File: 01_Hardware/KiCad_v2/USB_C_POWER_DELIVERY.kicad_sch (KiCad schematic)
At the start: 29 parts, among them Q200 SI7615DN-T1-GE3, Q201 SI7615DN-T1-GE3, Q202 DMP6050SSD, Q203 NVTA7002NT1G, U200 CYPD3177-24LQ

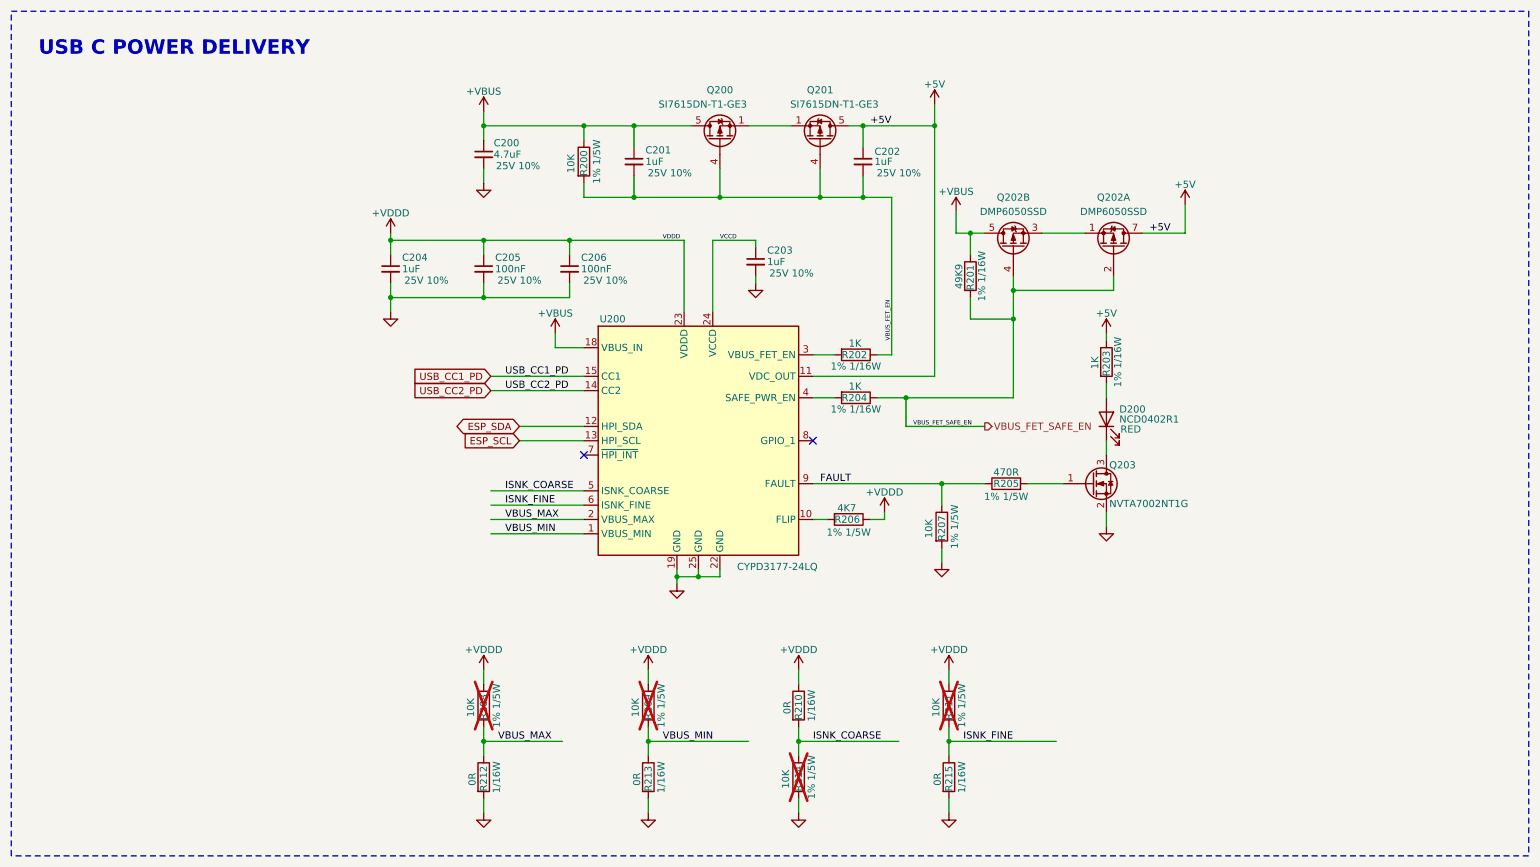
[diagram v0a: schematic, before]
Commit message: BOM done, except connectors/thermistor/button -> Will re-check BOM before sending to manufacturing
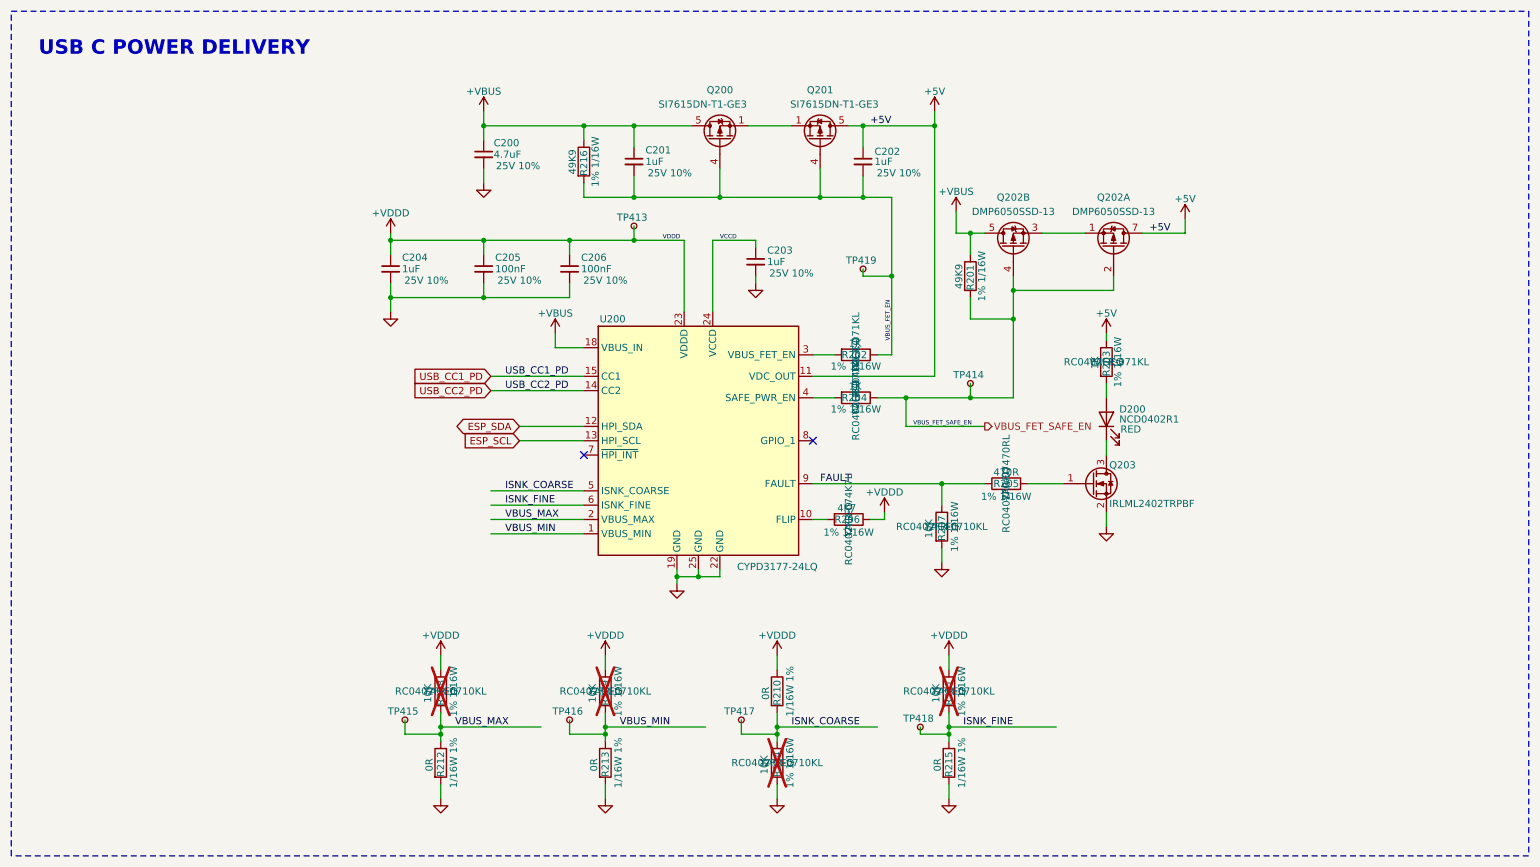
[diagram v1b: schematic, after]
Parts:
- removed R200: 10K, Resistor_SMD:R_0402_1005Metric, symbol Device:R
- added R216: 49K9, Resistor_SMD:R_0402_1005Metric, symbol Device:R
- added TP413, TP414, TP415, TP416, TP417, TP418, TP419: TestPoint_Small, TestPoint:TestPoint_Pad_D1.5mm, symbol Connector:TestPoint_Small
- C205, C206: Manufacturer Samsung Electro-Mechanics -> Samsung Electro-Mechanics
- D200: footprint Custom_Global_Footprints:SML-P13PTT_LED_0402_1005Metric -> LED_SMD:LED_0402_1005Metric
- Q202: value DMP6050SSD -> DMP6050SSD-13; Manufacturer Diodes Incorporated -> Diodes Incorporated
- Q203: value NVTA7002NT1G -> IRLML2402TRPBF; footprint Custom_Global_Footprints:NVTA7002N -> Package_TO_SOT_SMD:SOT-23; Link (none) -> https://jlcpcb.com/partdetail/InfineonTechnologies-IRLML240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; Manufacturer (none) -> Infineon Technologies; Manufacturer Part Number (none) -> IRLML2402TRPBF
- R201: Manufacturer (none) -> YAGEO; Manufacturer Part Number (none) -> RC0402FR-0749K9L
- R202, R203, R204: Manufacturer (none) -> YAGEO; Manufacturer Part Number (none) -> RC0402FR-071KL
- R205: Manufacturer (none) -> YAGEO; Manufacturer Part Number (none) -> RC0402FR-07470RL
- R206: Manufacturer (none) -> YAGEO; Manufacturer Part Number (none) -> RC0402FR-074K7L
- R207, R208, R209, R211, R214: Manufacturer (none) -> YAGEO; Manufacturer Part Number (none) -> RC0402FR-0710KL
- R210, R212, R213, R215: Manufacturer (none) -> YAGEO; Manufacturer Part Number (none) -> AC0402FR-070RL
- U200: Link (none) -> https://jlcpcb.com/partdetail/3345638-CYPD317724LQXQ/C29593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; Manufacturer (none) -> Infineon/Cypress Semicon; Manufacturer Part Number (none) -> CYPD3177-24LQXQ
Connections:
- net +VBUS: now also R216.1
- net +VDDD: now also TP413.1
- net ISNK_COARSE: now also TP417.1
- net ISNK_FINE: now also TP418.1
- net VBUS_FET_EN: now also R216.2, TP419.1
- net VBUS_FET_SAFE_EN: now also TP414.1
- net VBUS_MAX: now also TP415.1
- net VBUS_MIN: now also TP416.1
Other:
- moved on the sheet: R208, R209, R210, R211, R212, R213, R214, R215

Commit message: USB-C and Serial PCB routing done
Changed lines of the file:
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@@
 					(size 1.27 1.27)
 				)
+				(hide yes)
 			)
 		)
@@
 					(size 1.27 1.27)
 				)
+				(hide yes)
 			)
 		)
@@
 					(size 1.27 1.27)
 				)
+				(hide yes)
 			)
 		)
@@
 					(size 1.27 1.27)
 				)
+				(hide yes)
 			)
 		)
@@
 					(size 1.27 1.27)
 				)
+				(hide yes)
 			)
 		)
@@
 					(size 1.27 1.27)
 				)
+				(hide yes)
 			)
 		)
@@
 					(size 1.27 1.27)
 				)
+				(hide yes)
 			)
 		)
@@
 					(size 1.27 1.27)
 				)
+				(hide yes)
 			)
 		)
@@
 					(size 1.27 1.27)
 				)
+				(hide yes)
 			)
 		)
@@
 					(size 1.27 1.27)
 				)
+				(hide yes)
 			)
 		)
@@
 					(size 1.27 1.27)
 				)
+				(hide yes)
 			)
 		)
@@
 					(size 1.27 1.27)
 				)
+				(hide yes)
 			)
 		)
@@
 					(size 1.27 1.27)
 				)
+				(hide yes)
 			)
 		)
@@
 					(size 1.27 1.27)
 				)
+				(hide yes)
 			)
 		)
@@
 					(size 1.27 1.27)
 				)
+				(hide yes)
 			)
 		)
@@
 					(size 1.27 1.27)
 				)
+				(hide yes)
 			)
 		)
@@
 					(size 1.27 1.27)
 				)
+				(hide yes)
 			)
 		)
@@
 					(size 1.27 1.27)
 				)
+				(hide yes)
 			)
 		)
@@
 					(size 1.27 1.27)
 				)
+				(hide yes)
 			)
 		)
@@
 					(size 1.27 1.27)
 				)
+				(hide yes)
 			)
 		)
@@
 					(size 1.27 1.27)
 				)
+				(hide yes)
 			)
 		)
@@
 					(size 1.27 1.27)
 				)
+				(hide yes)
 			)
 		)
@@
 					(size 1.27 1.27)
 				)
+				(hide yes)
 			)
 		)
@@
 					(size 1.27 1.27)
 				)
+				(hide yes)
 			)
 		)
@@
 					(size 1.27 1.27)
 				)
+				(hide yes)
 			)
 		)
@@
 					(size 1.27 1.27)
 				)
+				(hide yes)
 			)
 		)
@@
 					(size 1.27 1.27)
 				)
+				(hide yes)
 			)
 		)
@@
 					(size 1.27 1.27)
 				)
+				(hide yes)
 			)
 		)
@@
 					(size 1.27 1.27)
 				)
+				(hide yes)
 			)
 		)
@@
 					(size 1.27 1.27)
 				)
+				(hide yes)
 			)
 		)

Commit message: PCB desing in progresssss
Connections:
- net VBUS_FET_EN: now also R202.2; no longer R202.1
- net at U200.3 (VBUS_FET_EN): now also R202.1; no longer R202.2
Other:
- moved on the sheet: R202
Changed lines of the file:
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@@
 					(size 1.27 1.27)
 				)
+				(hide yes)
 			)
 		)
@@
 					(size 1.27 1.27)
 				)
+				(hide yes)
 			)
 		)
@@
 					(size 1.27 1.27)
 				)
+				(hide yes)
 			)
 		)
@@
 					(size 1.27 1.27)
 				)
+				(hide yes)
 			)
 		)
@@
 					(size 1.27 1.27)
 				)
+				(hide yes)
 			)
 		)
@@
 					(size 1.27 1.27)
 				)
+				(hide yes)
 			)
 		)
@@
 					(size 1.27 1.27)
 				)
+				(hide yes)
 			)
 		)
@@
 					(size 1.27 1.27)
 				)
+				(hide yes)
 			)
 		)
@@
 					(size 1.27 1.27)
 				)
+				(hide yes)
 			)
 		)
@@
 					(size 1.27 1.27)
 				)
+				(hide yes)
 			)
 		)
@@
 					(size 1.27 1.27)
 				)
+				(hide yes)
 			)
 		)
@@
 					(size 1.27 1.27)
 				)
+				(hide yes)
 			)
 		)
@@
 	(symbol
 		(lib_id "Device:R")
-		(at 163.83 74.93 270)
+		(at 163.83 74.93 90)
+		(mirror x)
 		(unit 1)
 		(exclude_from_sim no)
@@
 		(dnp no)
 		(property "Reference" "R202"
-			(at 161.29 74.93 90)
+			(at 166.37 74.93 90)
 			(effects
 				(font
@@
 		)
 		(property "Value" "1K"
-			(at 162.56 72.898 90)
+			(at 165.1 72.898 90)
 			(effects
 				(font
@@
 					(size 1.27 1.27)
 				)
+				(hide yes)
 			)
 		)
@@
 					(size 1.27 1.27)
 				)
+				(hide yes)
 			)
 		)
@@
 					(size 1.27 1.27)
 				)
+				(hide yes)
 			)
 		)
@@
 					(size 1.27 1.27)
 				)
+				(hide yes)
 			)
 		)

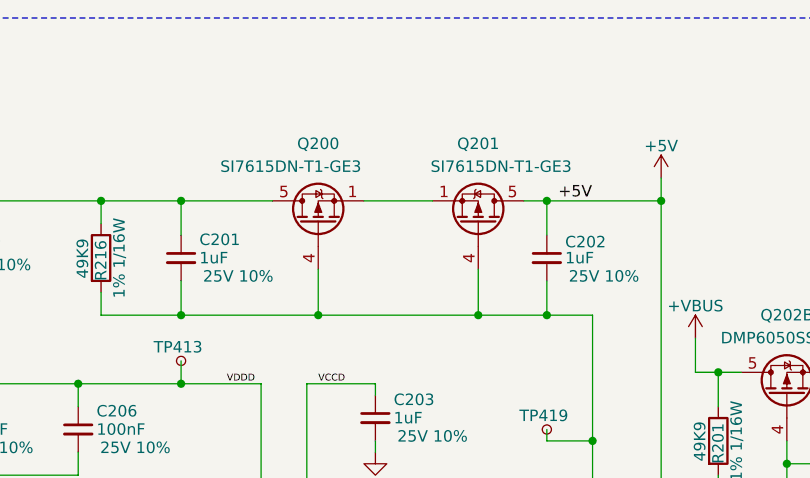
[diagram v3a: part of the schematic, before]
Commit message: Power plane/rearranged connectors
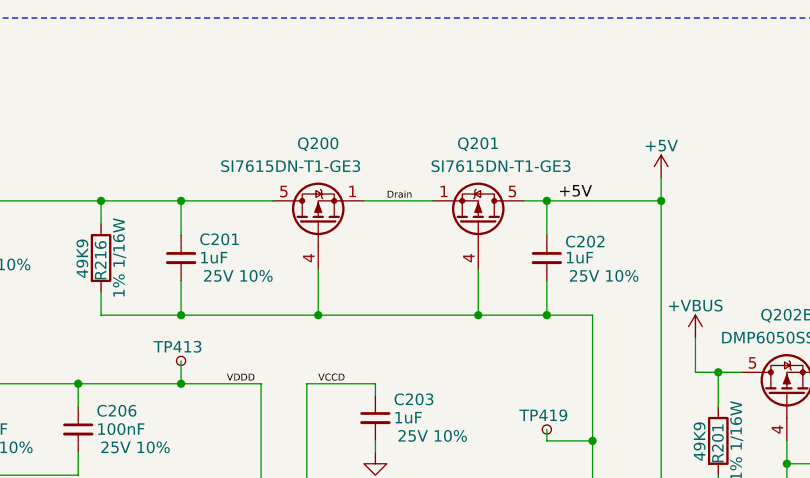
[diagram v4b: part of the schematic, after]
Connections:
- net Drain: now reaches Q200.1 (S), Q200.2 (S), Q200.3 (S), Q201.1 (S), Q201.2 (S), Q201.3 (S)
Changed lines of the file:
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@@
 		)
 	)
+	(label "Drain"
+		(at 147.32 34.29 0)
+		(effects
+			(font
+				(size 0.762 0.762)
+			)
+			(justify left bottom)
+		)
+	)
 	(global_label "ESP_SDA"
 		(shape bidirectional)
@@
 		(on_board yes)
 		(dnp no)
-		(fields_autoplaced yes)
 		(property "Reference" "U200"
 			(at 118.364 68.58 0)

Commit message: Hardware for manufacturing v0.2
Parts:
- removed TP415, TP416, TP417, TP418: TestPoint_Small, TestPoint:TestPoint_Pad_D1.5mm, symbol Connector:TestPoint_Small
- added F400, F401: Polyfuse_Small, Fuse:Fuse_1210_3225Metric, symbol Device:Polyfuse_Small
- C200: Manufacturer Samsung Electro-Mechanics -> (none); Manufacturer Part Number CL10A475KA8NQNC -> (none)
- TP413, TP414, TP419: footprint TestPoint:TestPoint_Pad_D1.5mm -> TestPoint:TestPoint_Pad_D1.0mm
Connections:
- net +5V: now also F400.2, F401.2; no longer C202.1, Q201.5 (D), Q202.7 (D1), Q202.8 (D1), U200.11 (VDC_OUT)
- new net Fuse_1A: F401.1, Q202.7 (D1), Q202.8 (D1)
- new net fuse_5A: C202.1, F400.1, Q201.5 (D), U200.11 (VDC_OUT)
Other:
- moved on the sheet: R208, R209, R210, R211, R212, R213, R214, R215
